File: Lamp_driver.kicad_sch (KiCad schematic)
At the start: 121 parts, among them J20 T44007, J21 T44007, J22 T44007, J23 Header, J24 T44007, Q20 MPF3N150, Q21 IXYH55N120, Q22 IXYH55N120, Q23 IXYH55N120, Q24 MDT7N65, U20 IRS2184

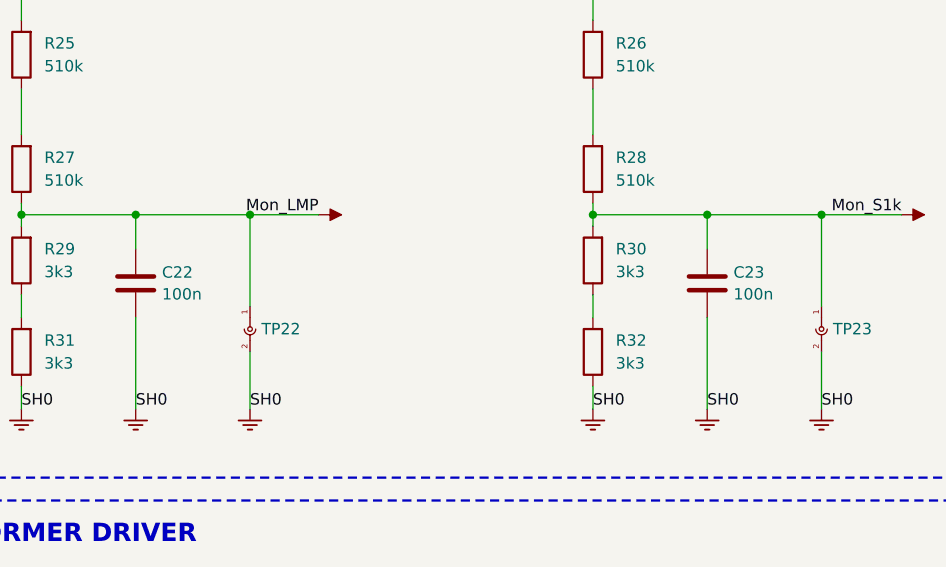
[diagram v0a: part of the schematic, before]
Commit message: Updated C22 and C23
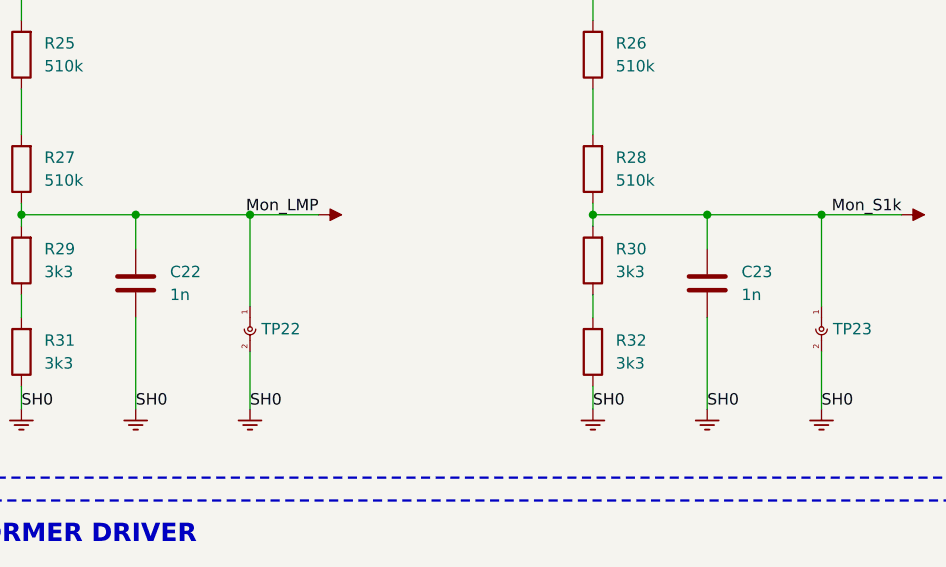
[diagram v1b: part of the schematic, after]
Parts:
- C22, C23: value 100n -> 1n
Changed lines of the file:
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@@
 		(fields_autoplaced yes)
 		(property "Reference" "C23"
-			(at 295.021 81.3379 0)
+			(at 295.91 81.2799 0)
 			(effects
 				(font
@@
 			)
 		)
-		(property "Value" "100n"
-			(at 295.021 83.7621 0)
+		(property "Value" "1n"
+			(at 295.91 83.8199 0)
 			(effects
 				(font
@@
 		(fields_autoplaced yes)
 		(property "Reference" "C22"
-			(at 231.521 81.3379 0)
+			(at 232.41 81.2799 0)
 			(effects
 				(font
@@
 			)
 		)
-		(property "Value" "100n"
-			(at 231.521 83.7621 0)
-			(effects
-				(font
+		(property "Value" "1n"
+			(at 232.41 83.8199 0)
+			(effects
+				(font
